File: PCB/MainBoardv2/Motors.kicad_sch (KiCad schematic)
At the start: 18 parts, among them J1 Screw_Terminal_01x02, J3 Screw_Terminal_01x02, J5 Screw_Terminal_01x02

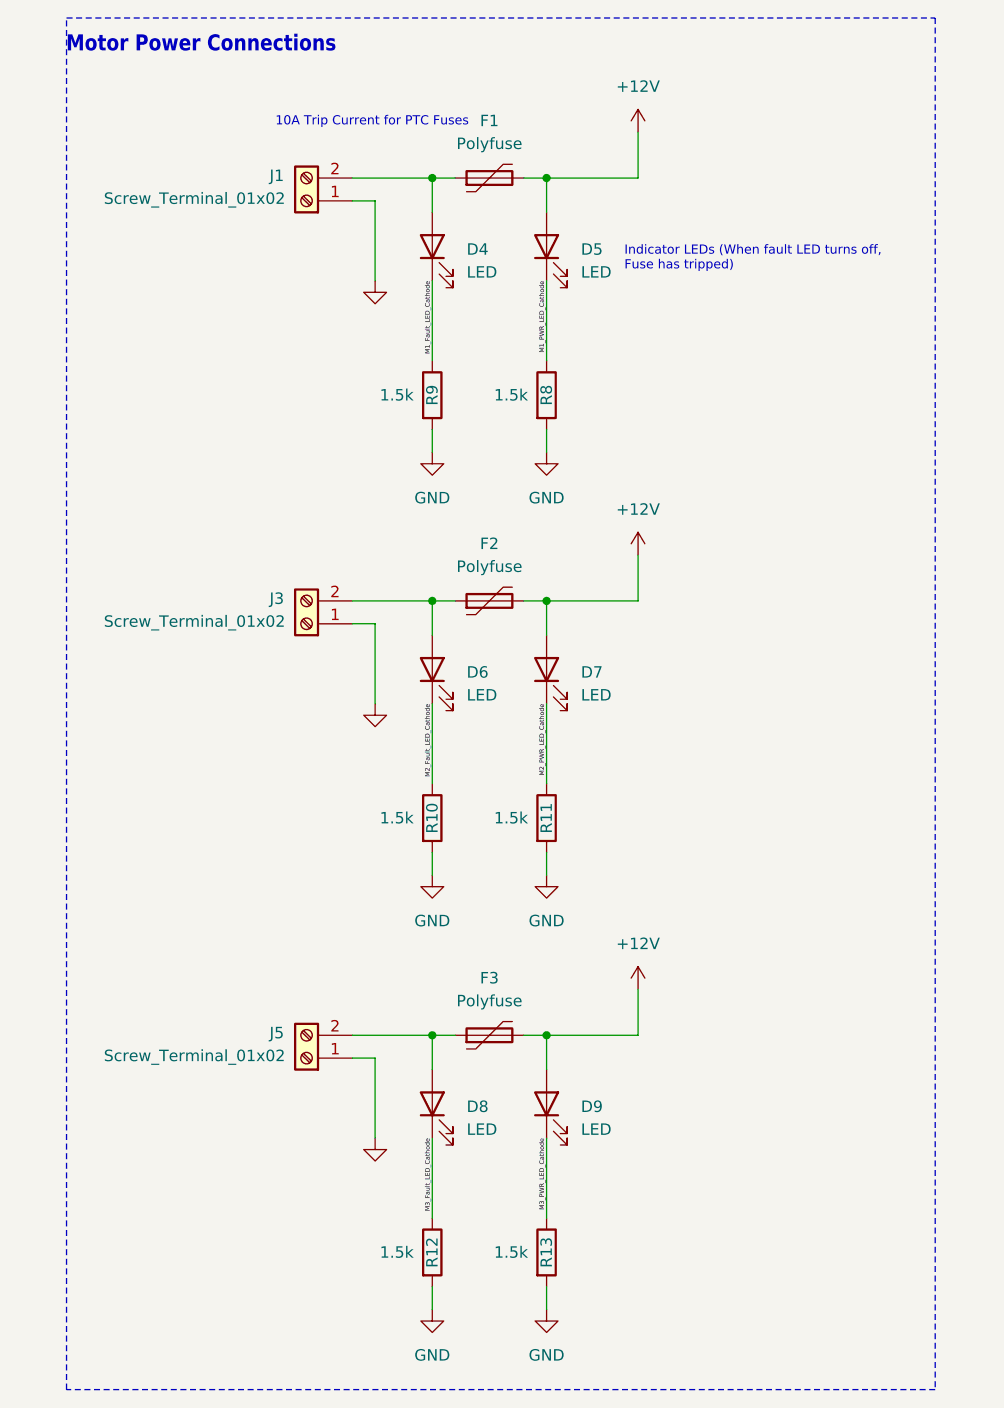
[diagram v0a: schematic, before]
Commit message: board v2 passing ERC in schematic
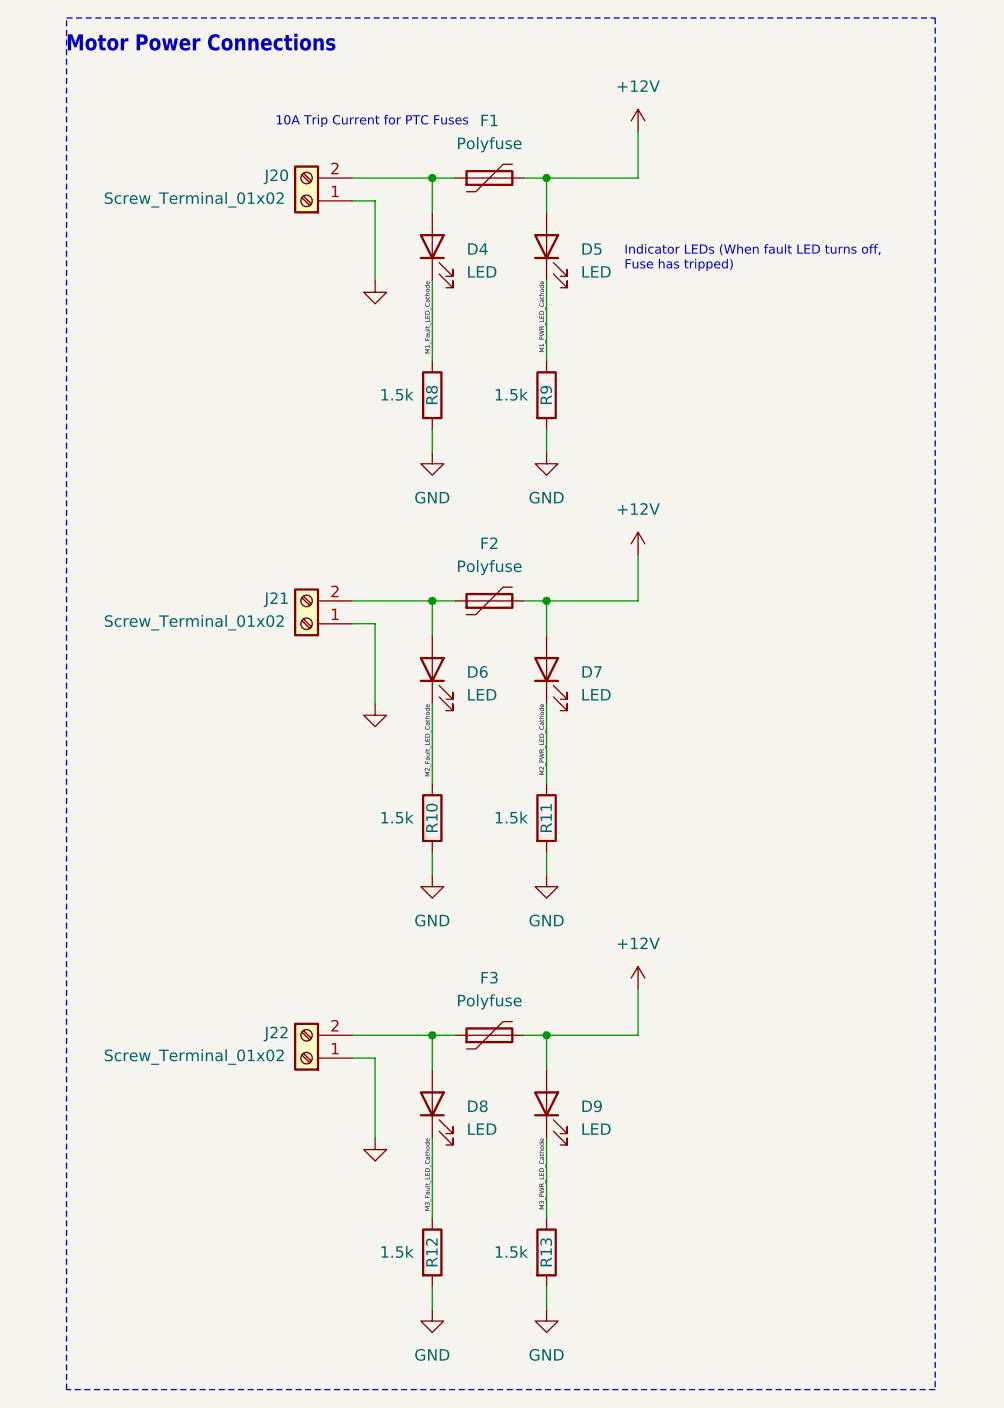
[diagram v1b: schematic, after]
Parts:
- renumbered J1 to J20, J3 to J21, J5 to J22, R9 to R8, R8 to R9
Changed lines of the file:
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@@
 	(title_block
 		(title "ECE445_MainBoard")
+		(date "2024-04-05")
 		(rev "2")
 		(company "University of Illinois Urbana-Champaign")
 		(comment 1 "ECE 445: Senior Design Lab")
+		(comment 2 "Rutvik Sayankar")
 	)
 	(junction
@@
 		(on_board yes)
 		(dnp no)
-		(property "Reference" "R9"
+		(property "Reference" "R8"
 			(at 78.74 68.58 90)
 			(effects
@@
 			(project "MainBoardv2"
 				(path "/d9c43b87-8960-41bd-bfcc-9c305bab2f72/0b6d272a-beab-45a0-995b-a46a98d72224"
-					(reference "R9")
+					(reference "R8")
 					(unit 1)
 				)
@@
 		(dnp no)
 		(fields_autoplaced yes)
-		(property "Reference" "#PWR021"
+		(property "Reference" "#PWR043"
 			(at 101.6 90.17 0)
 			(effects
@@
 			(project "MainBoardv2"
 				(path "/d9c43b87-8960-41bd-bfcc-9c305bab2f72/0b6d272a-beab-45a0-995b-a46a98d72224"
-					(reference "#PWR021")
+					(reference "#PWR043")
 					(unit 1)
 				)
@@
 		(on_board yes)
 		(dnp no)
-		(property "Reference" "R8"
+		(property "Reference" "R9"
 			(at 91.44 68.58 90)
 			(effects
@@
 			(project "MainBoardv2"
 				(path "/d9c43b87-8960-41bd-bfcc-9c305bab2f72/0b6d272a-beab-45a0-995b-a46a98d72224"
-					(reference "R8")
+					(reference "R9")
 					(unit 1)
 				)
@@
 		(dnp no)
 		(fields_autoplaced yes)
-		(property "Reference" "#PWR047"
+		(property "Reference" "#PWR040"
 			(at 72.39 62.23 0)
 			(effects
@@
 			(project "MainBoardv2"
 				(path "/d9c43b87-8960-41bd-bfcc-9c305bab2f72/0b6d272a-beab-45a0-995b-a46a98d72224"
-					(reference "#PWR047")
+					(reference "#PWR040")
 					(unit 1)
 				)
@@
 		(on_board yes)
 		(dnp no)
-		(property "Reference" "J5"
+		(property "Reference" "J22"
 			(at 61.468 139.446 0)
 			(effects
@@
 			(project "MainBoardv2"
 				(path "/d9c43b87-8960-41bd-bfcc-9c305bab2f72/0b6d272a-beab-45a0-995b-a46a98d72224"
-					(reference "J5")
+					(reference "J22")
 					(unit 1)
 				)
@@
 		(on_board yes)
 		(dnp no)
-		(property "Reference" "J1"
+		(property "Reference" "J20"
 			(at 61.468 44.196 0)
 			(effects
@@
 			(project "MainBoardv2"
 				(path "/d9c43b87-8960-41bd-bfcc-9c305bab2f72/0b6d272a-beab-45a0-995b-a46a98d72224"
-					(reference "J1")
+					(reference "J20")
 					(unit 1)
 				)
@@
 		(on_board yes)
 		(dnp no)
-		(property "Reference" "J3"
+		(property "Reference" "J21"
 			(at 61.468 91.186 0)
 			(effects
@@
 			(project "MainBoardv2"
 				(path "/d9c43b87-8960-41bd-bfcc-9c305bab2f72/0b6d272a-beab-45a0-995b-a46a98d72224"
-					(reference "J3")
+					(reference "J21")
 					(unit 1)
 				)
@@
 		(dnp no)
 		(fields_autoplaced yes)
-		(property "Reference" "#PWR043"
+		(property "Reference" "#PWR047"
 			(at 101.6 138.43 0)
 			(effects
@@
 			(project "MainBoardv2"
 				(path "/d9c43b87-8960-41bd-bfcc-9c305bab2f72/0b6d272a-beab-45a0-995b-a46a98d72224"
-					(reference "#PWR043")
+					(reference "#PWR047")
 					(unit 1)
 				)
@@
 		(dnp no)
 		(fields_autoplaced yes)
-		(property "Reference" "#PWR018"
+		(property "Reference" "#PWR039"
 			(at 101.6 43.18 0)
 			(effects
@@
 			(project "MainBoardv2"
 				(path "/d9c43b87-8960-41bd-bfcc-9c305bab2f72/0b6d272a-beab-45a0-995b-a46a98d72224"
-					(reference "#PWR018")
-					(unit 1)
-				)
+					(reference "#PWR039")
+					(unit 1)
+				)

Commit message: footprints all assigned for board v2
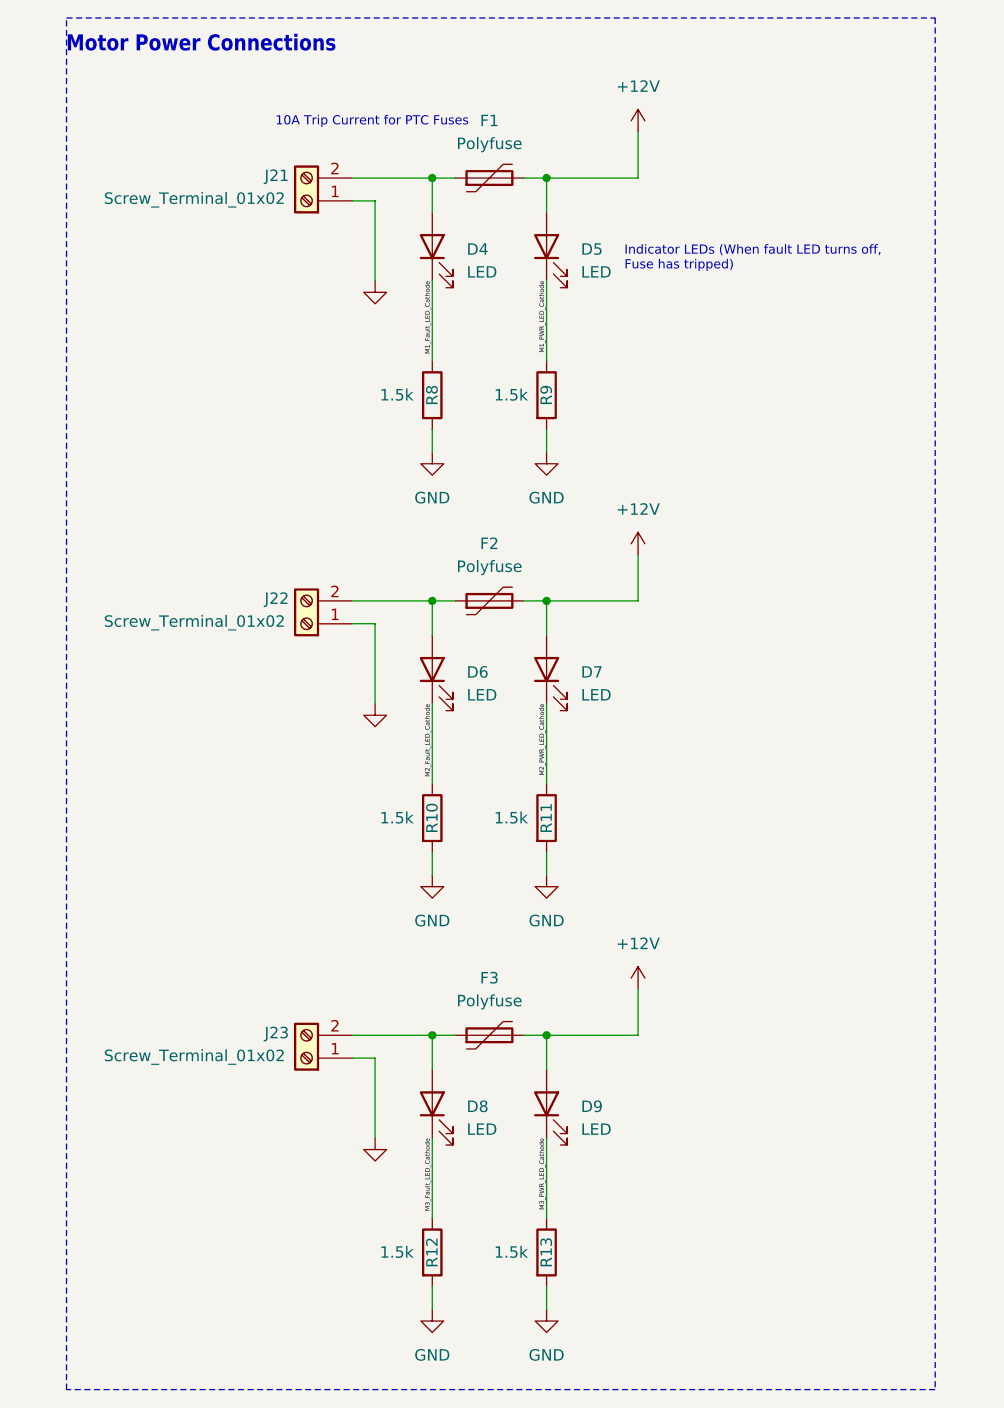
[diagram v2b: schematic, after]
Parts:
- D4, D5, D6, D7, D8, D9: footprint (none) -> LED_SMD:LED_0603_1608Metric
- J21: renamed from J20; footprint local:CONN_1985195 -> CustomFootprints:1985195
- J22: renamed from J21; footprint local:CONN_1985195 -> CustomFootprints:1985195
- J23: renamed from J22; footprint local:CONN_1985195 -> CustomFootprints:1985195

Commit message: pushing progress on mainboard v2 layout
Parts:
- J21, J22, J23: footprint CustomFootprints:1985195 -> CustomFootprints:PHOENIX_1017521
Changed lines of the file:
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@@
 			)
 		)
-		(property "Footprint" "CustomFootprints:1985195"
+		(property "Footprint" "CustomFootprints:PHOENIX_1017521"
 			(at 64.77 142.24 0)
 			(effects
@@
 			)
 		)
-		(property "Footprint" "CustomFootprints:1985195"
+		(property "Footprint" "CustomFootprints:PHOENIX_1017521"
 			(at 64.77 46.99 0)
 			(effects
@@
 			)
 		)
-		(property "Footprint" "CustomFootprints:1985195"
+		(property "Footprint" "CustomFootprints:PHOENIX_1017521"
 			(at 64.77 93.98 0)
 			(effects

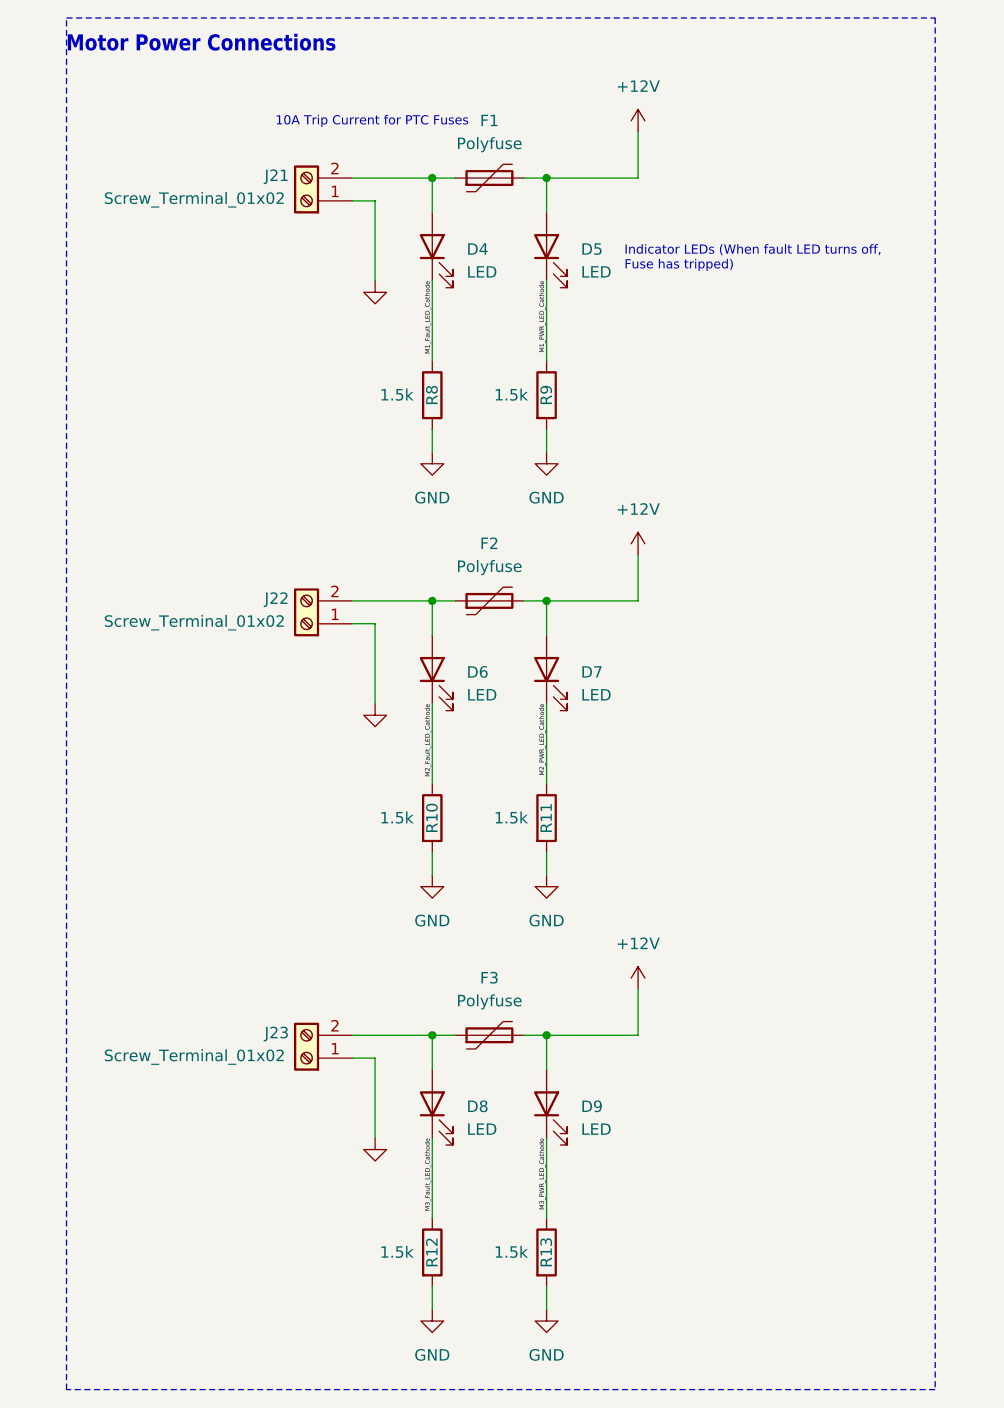
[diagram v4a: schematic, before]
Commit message: Main Board v2 Rough component layout complete
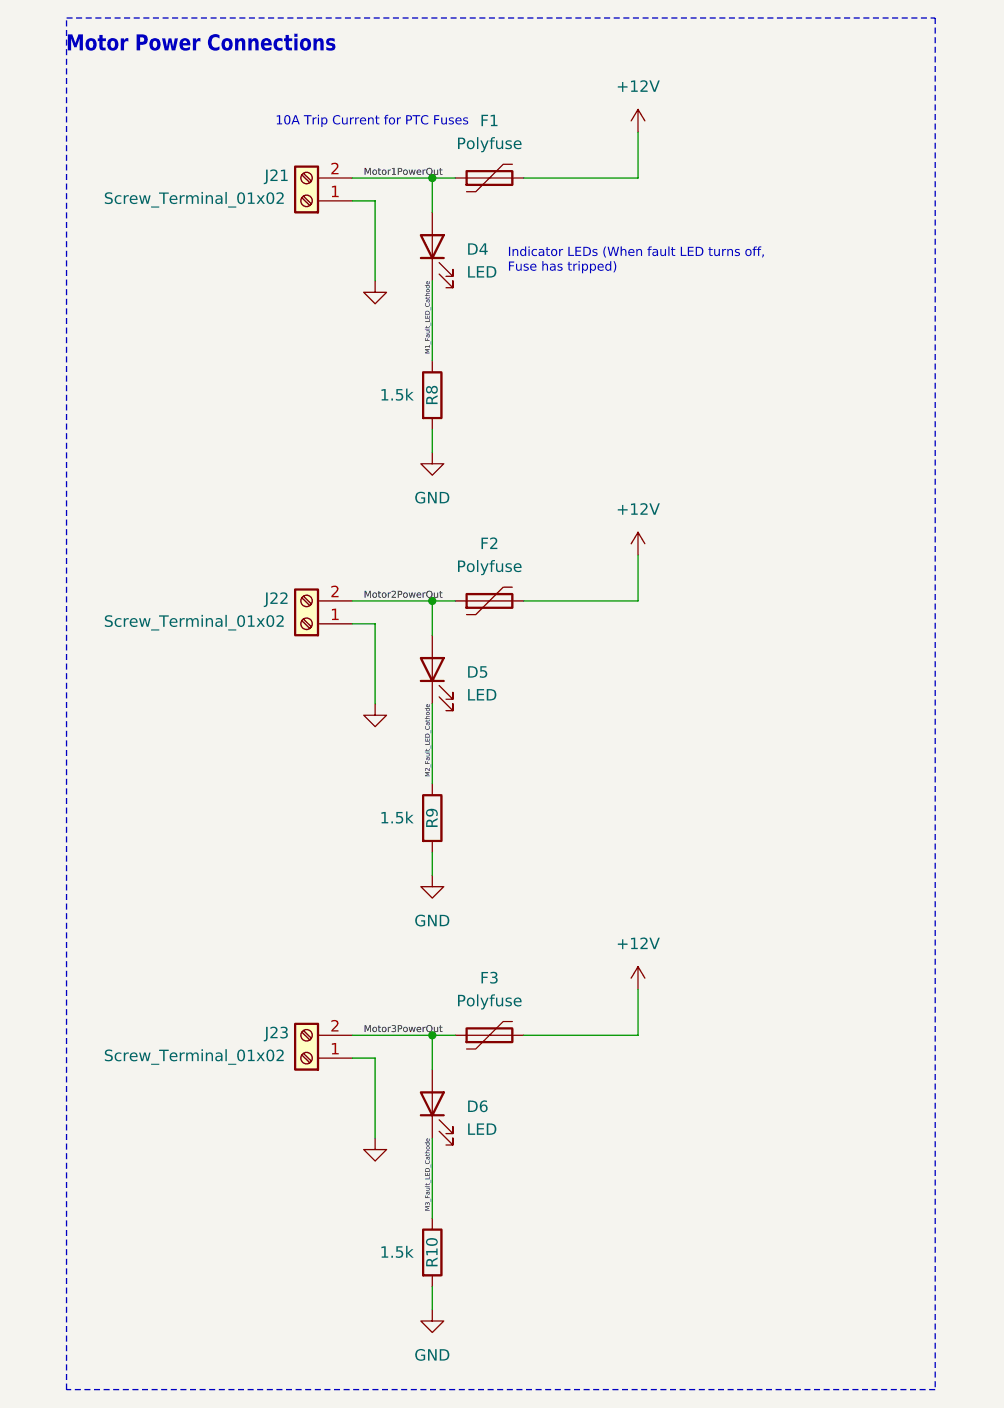
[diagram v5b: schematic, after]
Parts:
- removed D5, D7, D9: LED, LED_SMD:LED_0603_1608Metric, symbol Device:LED
- removed R11, R13, R9: 1.5k, Resistor_SMD:R_0603_1608Metric, symbol basic:R
- renumbered D6 to D5, D8 to D6, R12 to R10, R10 to R9
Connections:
- net Motor1PowerOut: now reaches D4.2 (A), F1.1, J21.2 (Pin_2)
- net Motor3PowerOut: now reaches D6.2 (A), F3.1, J23.2 (Pin_2)
- net Motor2PowerOut: now reaches D5.2 (A), F2.1, J22.2 (Pin_2)
